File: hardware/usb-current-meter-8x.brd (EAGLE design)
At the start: 94 x 44.5 mm, 154 parts, among them IC10 OPA2234U, IC12 LTC485S, IC2 OPA2234U, IC3 MEGA48/88/168-AU, IC4 OPA2234U, IC5 OPA2234U, IC6 OPA2234U, IC7 OPA2234U, IC8 OPA2234U, IC9 OPA2234U, U3 RJ45-8PTH, X1 MC2, X2 MC2, X3 MC2, X4 MC2, X5 MC2, X6 MC2, X7 MC2, X8 MC2

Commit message: 8x: progress save
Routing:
- net CH7: track 38.0 -> 36.0 mm
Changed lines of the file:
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@@
 <?xml version="1.0" encoding="utf-8"?>
 <!DOCTYPE eagle SYSTEM "eagle.dtd">
-<eagle version="6.2">
+<eagle version="6.1">
 <drawing>
 <settings>
@@
 <contactref element="C55" pad="2"/>
 <contactref element="R51" pad="1"/>
-<via x="58.1152" y="23.7744" extent="1-16" drill="0.508"/>
+<via x="57.3024" y="23.7744" extent="1-16" drill="0.508"/>
 <via x="53.0352" y="21.336" extent="1-16" drill="0.508"/>
 <via x="53.0352" y="22.5552" extent="1-16" drill="0.508"/>
@@
 <via x="48.5648" y="9.5504" extent="1-16" drill="0.508"/>
 <via x="48.5648" y="8.3312" extent="1-16" drill="0.508"/>
+<via x="58.928" y="23.7744" extent="1-16" drill="0.508"/>
 </signal>
 <signal name="N$1">
@@
 <wire x1="78.8416" y1="21.402" x2="78.8416" y2="19.7104" width="0.4064" layer="16"/>
 <via x="78.8416" y="19.7104" extent="1-16" drill="0.508"/>
-<wire x1="59.944" y1="23.9776" x2="59.5376" y2="23.5712" width="0.4064" layer="1"/>
-<wire x1="56.919053125" y1="17.833196875" x2="59.5376" y2="20.45174375" width="0.4064" layer="1"/>
-<wire x1="59.5376" y1="20.45174375" x2="59.5376" y2="23.5712" width="0.4064" layer="1"/>
-<wire x1="75.5904" y1="22.352" x2="75.5904" y2="21.1328" width="0.4064" layer="1"/>
-<wire x1="75.5904" y1="21.1328" x2="77.0128" y2="19.7104" width="0.4064" layer="1"/>
+<wire x1="60.5536" y1="23.368" x2="60.1472" y2="22.9616" width="0.4064" layer="1"/>
+<wire x1="56.919053125" y1="17.833196875" x2="60.1472" y2="21.06134375" width="0.4064" layer="1"/>
+<wire x1="60.1472" y1="21.06134375" x2="60.1472" y2="22.9616" width="0.4064" layer="1"/>
+<wire x1="73.3552" y1="23.368" x2="77.0128" y2="19.7104" width="0.4064" layer="1"/>
 <wire x1="78.8416" y1="19.7104" x2="77.0128" y2="19.7104" width="0.4064" layer="1"/>
-<wire x1="73.9648" y1="23.9776" x2="75.5904" y2="22.352" width="0.4064" layer="1"/>
-<wire x1="59.944" y1="23.9776" x2="73.9648" y2="23.9776" width="0.4064" layer="1"/>
+<wire x1="60.5536" y1="23.368" x2="73.3552" y2="23.368" width="0.4064" layer="1"/>
 </signal>
 <signal name="UART_EN">
@@
 <wire x1="48.768" y1="31.496" x2="48.3616" y2="31.0896" width="0.4064" layer="16"/>
 <wire x1="48.3616" y1="31.0896" x2="48.3616" y2="26.6192" width="0.4064" layer="16"/>
-<via x="61.1632" y="22.9616" extent="1-16" drill="0.508"/>
+<via x="61.1632" y="22.352" extent="1-16" drill="0.508"/>
 <wire x1="48.3616" y1="26.6192" x2="49.784" y2="25.1968" width="0.4064" layer="16"/>
 <wire x1="49.784" y1="25.1968" x2="60.1472" y2="25.1968" width="0.4064" layer="16"/>
-<wire x1="61.1632" y1="24.1808" x2="61.1632" y2="22.9616" width="0.4064" layer="16"/>
+<wire x1="61.1632" y1="24.1808" x2="61.1632" y2="22.352" width="0.4064" layer="16"/>
 <wire x1="60.1472" y1="25.1968" x2="61.1632" y2="24.1808" width="0.4064" layer="16"/>
 <contactref element="IC3" pad="17"/>
 <wire x1="58.050425" y1="16.701825" x2="61.1632" y2="19.8146" width="0.3048" layer="1"/>
-<wire x1="61.1632" y1="19.8146" x2="61.1632" y2="22.9616" width="0.3048" layer="1"/>
+<wire x1="61.1632" y1="19.8146" x2="61.1632" y2="22.352" width="0.3048" layer="1"/>
 <contactref element="ISP1" pad="3"/>
-<wire x1="61.1632" y1="22.9616" x2="61.976" y2="22.1488" width="0.2032" layer="16"/>
-<wire x1="61.976" y1="22.1488" x2="63.3984" y2="22.1488" width="0.2032" layer="16"/>
-<wire x1="63.3984" y1="22.1488" x2="66.04" y2="19.5072" width="0.2032" layer="16"/>
-<via x="66.04" y="19.5072" extent="1-16" drill="0.508"/>
+<wire x1="61.1632" y1="22.352" x2="61.976" y2="21.5392" width="0.2032" layer="16"/>
+<wire x1="61.976" y1="21.5392" x2="64.008" y2="21.5392" width="0.2032" layer="16"/>
+<wire x1="64.008" y1="21.5392" x2="66.8528" y2="18.6944" width="0.2032" layer="16"/>
+<via x="66.8528" y="18.6944" extent="1-16" drill="0.508"/>
 <wire x1="69.6976" y1="16.3068" x2="69.6976" y2="17.272" width="0.2032" layer="1"/>
-<wire x1="67.4624" y1="19.5072" x2="66.04" y2="19.5072" width="0.2032" layer="1"/>
-<wire x1="69.6976" y1="17.272" x2="67.4624" y2="19.5072" width="0.2032" layer="1"/>
+<wire x1="68.2752" y1="18.6944" x2="66.8528" y2="18.6944" width="0.2032" layer="1"/>
+<wire x1="69.6976" y1="17.272" x2="68.2752" y2="18.6944" width="0.2032" layer="1"/>
 </signal>
 <signal name="CH5_GAIN">
@@
 <wire x1="58.5216" y1="31.496" x2="58.1152" y2="31.0896" width="0.4064" layer="16"/>
 <wire x1="58.1152" y1="31.0896" x2="58.1152" y2="26.8224" width="0.4064" layer="16"/>
-<via x="62.5856" y="22.9616" extent="1-16" drill="0.508"/>
+<via x="62.5856" y="22.352" extent="1-16" drill="0.508"/>
 <wire x1="58.1152" y1="26.8224" x2="58.5216" y2="26.416" width="0.4064" layer="16"/>
 <wire x1="58.5216" y1="26.416" x2="60.3504" y2="26.416" width="0.4064" layer="16"/>
 <wire x1="60.3504" y1="26.416" x2="62.5856" y2="24.1808" width="0.4064" layer="16"/>
-<wire x1="62.5856" y1="24.1808" x2="62.5856" y2="22.9616" width="0.4064" layer="16"/>
+<wire x1="62.5856" y1="24.1808" x2="62.5856" y2="22.352" width="0.4064" layer="16"/>
 <contactref element="IC3" pad="16"/>
 <wire x1="58.050425" y1="14.590971875" x2="59.5376" y2="16.078146875" width="0.3048" layer="1"/>
 <wire x1="59.5376" y1="16.078146875" x2="59.5376" y2="17.0688" width="0.3048" layer="1"/>
 <wire x1="59.5376" y1="17.0688" x2="62.5856" y2="20.1168" width="0.3048" layer="1"/>
-<wire x1="62.5856" y1="20.1168" x2="62.5856" y2="22.9616" width="0.3048" layer="1"/>
+<wire x1="62.5856" y1="20.1168" x2="62.5856" y2="22.352" width="0.3048" layer="1"/>
 <contactref element="ISP1" pad="1"/>
-<via x="67.056" y="20.5232" extent="1-16" drill="0.508"/>
-<wire x1="67.056" y1="20.5232" x2="65.8368" y2="20.5232" width="0.2032" layer="16"/>
-<wire x1="65.8368" y1="20.5232" x2="63.3984" y2="22.9616" width="0.2032" layer="16"/>
-<wire x1="63.3984" y1="22.9616" x2="62.5856" y2="22.9616" width="0.2032" layer="16"/>
-<wire x1="71.0184" y1="16.764" x2="70.9168" y2="16.8656" width="0.2032" layer="1"/>
-<wire x1="70.9168" y1="16.8656" x2="67.2592" y2="20.5232" width="0.2032" layer="1"/>
-<wire x1="67.2592" y1="20.5232" x2="67.056" y2="20.5232" width="0.2032" layer="1"/>
+<via x="67.8688" y="19.7104" extent="1-16" drill="0.508"/>
+<wire x1="67.8688" y1="19.7104" x2="66.6496" y2="19.7104" width="0.2032" layer="16"/>
+<wire x1="66.6496" y1="19.7104" x2="64.008" y2="22.352" width="0.2032" layer="16"/>
+<wire x1="64.008" y1="22.352" x2="62.5856" y2="22.352" width="0.2032" layer="16"/>
+<wire x1="71.4756" y1="16.3068" x2="68.072" y2="19.7104" width="0.2032" layer="1"/>
+<wire x1="68.072" y1="19.7104" x2="67.8688" y2="19.7104" width="0.2032" layer="1"/>
 <wire x1="72.2376" y1="16.3068" x2="71.4756" y2="16.3068" width="0.2032" layer="1"/>
-<wire x1="71.4756" y1="16.3068" x2="71.0184" y2="16.764" width="0.2032" layer="1"/>
 </signal>
 <signal name="CH6_GAIN">
@@
 <wire x1="68.2752" y1="34.544" x2="68.2752" y2="31.496" width="0.4064" layer="16"/>
 <wire x1="68.2752" y1="31.496" x2="67.8688" y2="31.0896" width="0.4064" layer="16"/>
-<wire x1="67.8688" y1="31.0896" x2="67.8688" y2="22.9616" width="0.4064" layer="16"/>
-<via x="67.8688" y="22.9616" extent="1-16" drill="0.508"/>
+<wire x1="67.8688" y1="31.0896" x2="67.8688" y2="22.352" width="0.4064" layer="16"/>
+<via x="67.8688" y="22.352" extent="1-16" drill="0.508"/>
 <contactref element="IC3" pad="14"/>
 <wire x1="56.919053125" y1="13.4596" x2="57.577053125" y2="12.8016" width="0.3048" layer="1"/>
@@
 <wire x1="58.928" y1="12.8016" x2="60.7568" y2="14.6304" width="0.3048" layer="1"/>
 <wire x1="60.7568" y1="14.6304" x2="60.7568" y2="17.0688" width="0.3048" layer="1"/>
-<wire x1="60.7568" y1="17.0688" x2="66.6496" y2="22.9616" width="0.3048" layer="1"/>
-<wire x1="66.6496" y1="22.9616" x2="67.8688" y2="22.9616" width="0.3048" layer="1"/>
+<wire x1="60.7568" y1="17.0688" x2="66.04" y2="22.352" width="0.3048" layer="1"/>
+<wire x1="66.04" y1="22.352" x2="67.8688" y2="22.352" width="0.3048" layer="1"/>
 </signal>
 <signal name="CH7_GAIN">
@@
 <via x="78.0288" y="28.0416" extent="1-16" drill="0.508"/>
 <wire x1="78.0288" y1="28.0416" x2="78.0288" y2="25.8064" width="0.4064" layer="16"/>
-<via x="73.9648" y="21.7424" extent="1-16" drill="0.508"/>
+<via x="73.5584" y="21.336" extent="1-16" drill="0.508"/>
 <contactref element="IC3" pad="13"/>
 <wire x1="56.35336875" y1="12.893915625" x2="57.055284375" y2="12.192" width="0.3048" layer="1"/>
@@
 <wire x1="59.1312" y1="12.192" x2="61.5696" y2="14.6304" width="0.3048" layer="1"/>
 <wire x1="61.5696" y1="14.6304" x2="61.5696" y2="16.8656" width="0.3048" layer="1"/>
-<wire x1="61.5696" y1="16.8656" x2="66.4464" y2="21.7424" width="0.3048" layer="1"/>
-<wire x1="66.4464" y1="21.7424" x2="73.9648" y2="21.7424" width="0.3048" layer="1"/>
-<wire x1="78.0288" y1="25.8064" x2="73.9648" y2="21.7424" width="0.4064" layer="16"/>
+<wire x1="61.5696" y1="16.8656" x2="66.04" y2="21.336" width="0.3048" layer="1"/>
+<wire x1="66.04" y1="21.336" x2="73.5584" y2="21.336" width="0.3048" layer="1"/>
+<wire x1="78.0288" y1="25.8064" x2="73.5584" y2="21.336" width="0.4064" layer="16"/>
 </signal>
 <signal name="UART_TX">

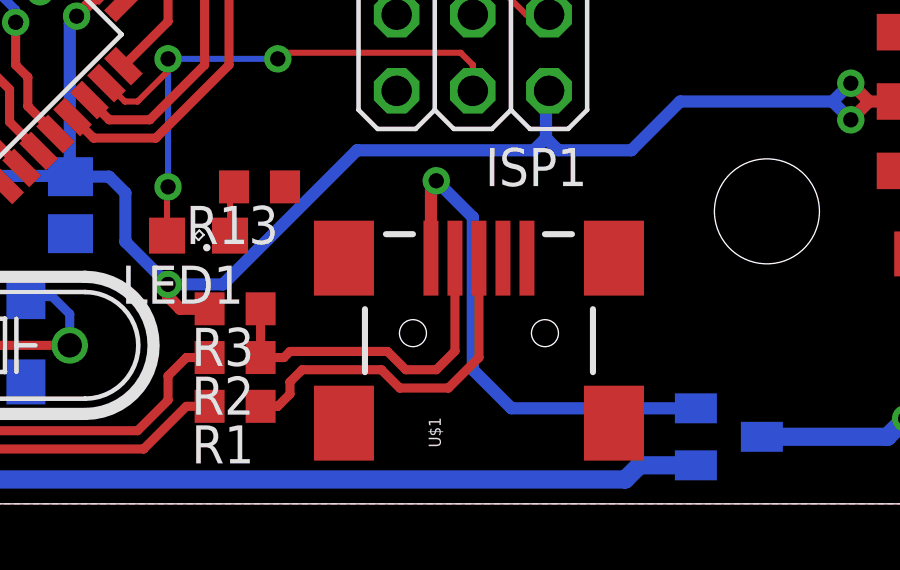
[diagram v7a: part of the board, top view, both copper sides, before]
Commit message: 8x: moved usb connector into the board
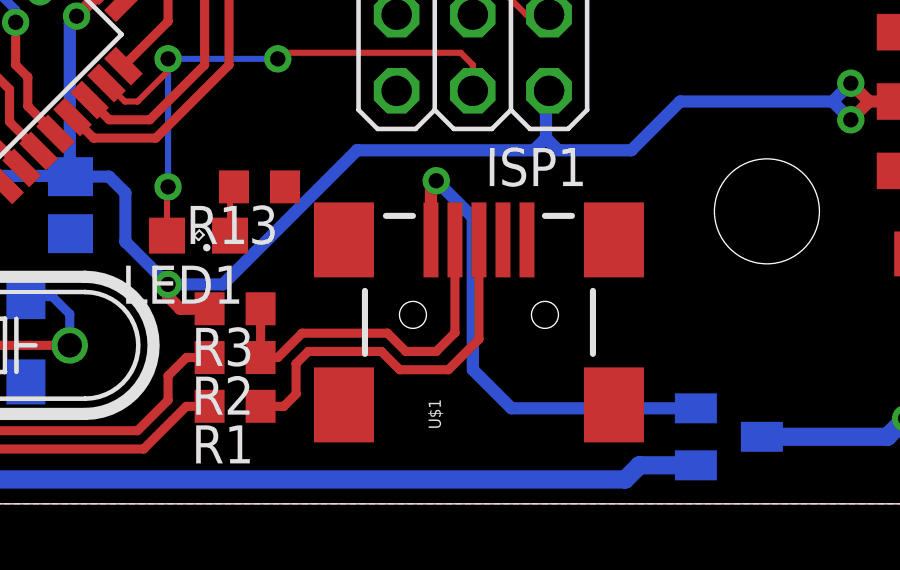
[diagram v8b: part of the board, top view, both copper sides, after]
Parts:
- moved U$1 0.61 mm to (69.9, 6.30)
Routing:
- net VIN_USB: track 17.4 -> 16.8 mm
- net N$2: track 12.0 -> 12.6 mm
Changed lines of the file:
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@@
 <element name="R13" library="rcl" package="R0603" value="330" x="62.5856" y="10.5664" rot="R180"/>
 <element name="ISP1" library="balto" package="2X03" value="" x="69.6976" y="15.0368" rot="R180"/>
-<element name="U$1" library="SparkFun" package="USB-MINIB" value="USB-MINIB-5PIN" x="69.9008" y="5.6896" rot="R90"/>
+<element name="U$1" library="SparkFun" package="USB-MINIB" value="USB-MINIB-5PIN" x="69.9008" y="6.2992" rot="R90"/>
 <element name="Y1" library="SparkFun" package="HC49U-V" value="" x="53.848" y="5.2832"/>
 <element name="C9" library="rcl" package="C0805" value=".1u" x="58.1152" y="22.1488" rot="R90"/>
@@
 <contactref element="R3" pad="1"/>
 <contactref element="U$1" pad="D-"/>
-<wire x1="63.6016" y1="5.08" x2="66.8528" y2="5.08" width="0.3048" layer="1"/>
-<wire x1="66.8528" y1="5.08" x2="67.4624" y2="4.4704" width="0.3048" layer="1"/>
-<wire x1="67.4624" y1="4.4704" x2="68.4784" y2="4.4704" width="0.3048" layer="1"/>
-<wire x1="68.4784" y1="4.4704" x2="69.1008" y2="5.0928" width="0.3048" layer="1"/>
-<wire x1="69.1008" y1="8.1896" x2="69.1008" y2="5.0928" width="0.3048" layer="1"/>
+<wire x1="64.008" y1="5.6896" x2="66.8528" y2="5.6896" width="0.3048" layer="1"/>
+<wire x1="66.8528" y1="5.6896" x2="67.4624" y2="5.08" width="0.3048" layer="1"/>
+<wire x1="67.4624" y1="5.08" x2="68.4784" y2="5.08" width="0.3048" layer="1"/>
+<wire x1="68.4784" y1="5.08" x2="69.1008" y2="5.7024" width="0.3048" layer="1"/>
+<wire x1="69.1008" y1="8.7992" x2="69.1008" y2="5.7024" width="0.3048" layer="1"/>
 <wire x1="62.6228" y1="4.8768" x2="62.6228" y2="6.5024" width="0.3048" layer="1"/>
-<wire x1="62.6228" y1="4.8768" x2="63.3984" y2="4.8768" width="0.3048" layer="1"/>
-<wire x1="63.3984" y1="4.8768" x2="63.6016" y2="5.08" width="0.3048" layer="1"/>
+<wire x1="62.6228" y1="4.8768" x2="63.1952" y2="4.8768" width="0.3048" layer="1"/>
+<wire x1="63.1952" y1="4.8768" x2="64.008" y2="5.6896" width="0.3048" layer="1"/>
 </signal>
 <signal name="N$2">
 <contactref element="R1" pad="1"/>
 <contactref element="U$1" pad="D+"/>
-<wire x1="64.008" y1="4.4704" x2="66.6496" y2="4.4704" width="0.3048" layer="1"/>
-<wire x1="66.6496" y1="4.4704" x2="67.2592" y2="3.8608" width="0.3048" layer="1"/>
-<wire x1="67.2592" y1="3.8608" x2="68.8848" y2="3.8608" width="0.3048" layer="1"/>
-<wire x1="68.8848" y1="3.8608" x2="69.9008" y2="4.8768" width="0.3048" layer="1"/>
-<wire x1="69.9008" y1="8.1896" x2="69.9008" y2="4.8768" width="0.3048" layer="1"/>
-<wire x1="62.6228" y1="3.2512" x2="63.1952" y2="3.2512" width="0.3048" layer="1"/>
-<wire x1="63.1952" y1="3.2512" x2="63.6016" y2="3.6576" width="0.3048" layer="1"/>
-<wire x1="63.6016" y1="3.6576" x2="63.6016" y2="4.064" width="0.3048" layer="1"/>
-<wire x1="64.008" y1="4.4704" x2="63.6016" y2="4.064" width="0.3048" layer="1"/>
+<wire x1="64.2112" y1="5.08" x2="66.6496" y2="5.08" width="0.3048" layer="1"/>
+<wire x1="66.6496" y1="5.08" x2="67.2592" y2="4.4704" width="0.3048" layer="1"/>
+<wire x1="67.2592" y1="4.4704" x2="68.8848" y2="4.4704" width="0.3048" layer="1"/>
+<wire x1="68.8848" y1="4.4704" x2="69.9008" y2="5.4864" width="0.3048" layer="1"/>
+<wire x1="69.9008" y1="8.7992" x2="69.9008" y2="5.4864" width="0.3048" layer="1"/>
+<wire x1="64.2112" y1="5.08" x2="63.8048" y2="4.6736" width="0.3048" layer="1"/>
+<wire x1="63.8048" y1="4.6736" x2="63.8048" y2="3.6576" width="0.3048" layer="1"/>
+<wire x1="63.8048" y1="3.6576" x2="63.3984" y2="3.2512" width="0.3048" layer="1"/>
+<wire x1="63.3984" y1="3.2512" x2="62.6228" y2="3.2512" width="0.3048" layer="1"/>
 </signal>
 <signal name="+5V">
@@
 <contactref element="U$1" pad="VBUS"/>
 <contactref element="D9" pad="2"/>
-<wire x1="68.3008" y1="8.1896" x2="68.3008" y2="10.592" width="0.4064" layer="1"/>
+<wire x1="68.3008" y1="8.7992" x2="68.3008" y2="10.592" width="0.4064" layer="1"/>
 <wire x1="68.3008" y1="10.592" x2="68.4784" y2="10.7696" width="0.4064" layer="1"/>
 <via x="68.4784" y="10.7696" extent="1-16" drill="0.508"/>
